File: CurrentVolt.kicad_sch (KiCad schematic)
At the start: 3 parts, among them U6 ACS70331EOLCTR-2P5U3

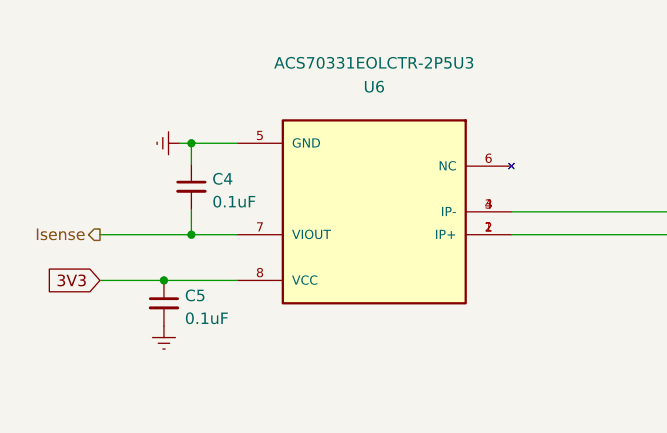
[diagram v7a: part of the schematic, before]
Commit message: new EMC-EMI layout with improved suppression
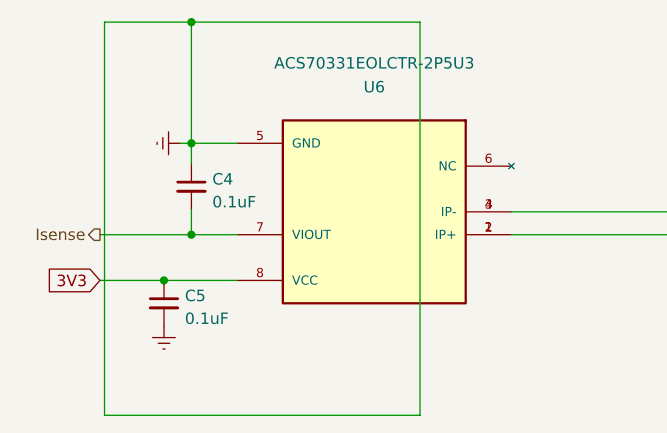
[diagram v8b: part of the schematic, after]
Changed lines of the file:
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@@
   (junction (at 81.28 81.28) (diameter 0) (color 0 0 0 0)
+  )
+  (junction (at 81.28 67.818) (diameter 0) (color 0 0 0 0)
   )
   (junction (at 78.232 96.52) (diameter 0) (color 0 0 0 0)
@@
     (stroke (width 0) (type default) (color 0 0 0 0))
   )
+  (wire (pts (xy 106.68 67.818) (xy 106.68 111.506))
+    (stroke (width 0) (type default) (color 0 0 0 0))
+  )
   (wire (pts (xy 71.12 91.44) (xy 81.28 91.44))
     (stroke (width 0) (type default) (color 0 0 0 0))
@@
     (stroke (width 0) (type default) (color 0 0 0 0))
   )
+  (wire (pts (xy 71.628 67.818) (xy 71.628 111.506))
+    (stroke (width 0) (type default) (color 0 0 0 0))
+  )
+  (wire (pts (xy 71.628 67.818) (xy 81.28 67.818))
+    (stroke (width 0) (type default) (color 0 0 0 0))
+  )
   (wire (pts (xy 81.28 88.646) (xy 81.28 91.44))
     (stroke (width 0) (type default) (color 0 0 0 0))
@@
     (stroke (width 0) (type default) (color 0 0 0 0))
   )
+  (wire (pts (xy 81.28 67.818) (xy 106.68 67.818))
+    (stroke (width 0) (type default) (color 0 0 0 0))
+  )
   (wire (pts (xy 116.84 91.44) (xy 162.56 91.44))
+    (stroke (width 0) (type default) (color 0 0 0 0))
+  )
+  (wire (pts (xy 81.28 67.818) (xy 81.28 81.28))
     (stroke (width 0) (type default) (color 0 0 0 0))
   )
@@
     (stroke (width 0) (type default) (color 0 0 0 0))
   )
+  (wire (pts (xy 106.68 111.506) (xy 71.628 111.506))
+    (stroke (width 0) (type default) (color 0 0 0 0))
+  )
